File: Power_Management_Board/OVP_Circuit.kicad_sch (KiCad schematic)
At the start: 4 parts, among them Q2 DMG3406L-7, U4 TPS2400

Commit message: Finished USB-C Power Board Design
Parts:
- C10: footprint (none) -> Capacitor_SMD:C_0603_1608Metric_Pad1.08x0.95mm_HandSolder
- D5: value D_Zener -> NC
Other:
- note added: "30V Tolerant"
- note added: "Components need to be at least 20V tolerant"
- note added: "Zener Diode attenuates the voltage spike from an inductive power supply when load is disconnected. Most likely optional"
- note removed: "Zener Diode attenuates the voltage spike from an inductive power supply when load is disconnected."
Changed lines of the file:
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@@
+		)
+	)
+	(text "30V Tolerant"
+		(exclude_from_sim no)
+		(at 114.808 46.736 0)
+		(effects
+			(font
+				(size 1.27 1.27)
+			)
 		)
 	)
@@
 		)
 	)
-	(text "Zener Diode attenuates the voltage\nspike from an inductive power \nsupply when load is disconnected."
+	(text "Components need to be \nat least 20V tolerant"
 		(exclude_from_sim no)
-		(at 27.94 67.31 0)
+		(at 67.31 44.704 0)
+		(effects
+			(font
+				(size 1.27 1.27)
+			)
+		)
+	)
+	(text "Zener Diode attenuates the voltage\nspike from an inductive power \nsupply when load is disconnected.\nMost likely optional"
+		(exclude_from_sim no)
+		(at 26.924 70.612 0)
 		(effects
 			(font
@@
 			)
 		)
-		(property "Footprint" ""
+		(property "Footprint" "Capacitor_SMD:C_0603_1608Metric_Pad1.08x0.95mm_HandSolder"
 			(at 68.58 54.61 0)
 			(effects
@@
 			)
 		)
-		(property "Value" "D_Zener"
+		(property "Value" "NC"
 			(at 49.53 57.15 90)
 			(effects

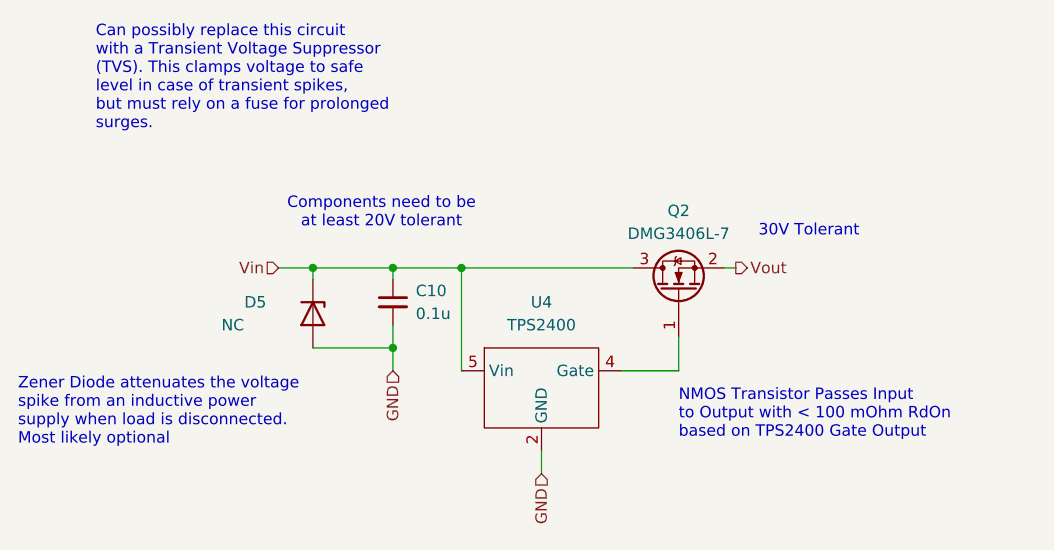
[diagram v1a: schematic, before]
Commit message: Raspberry Pi Board Added
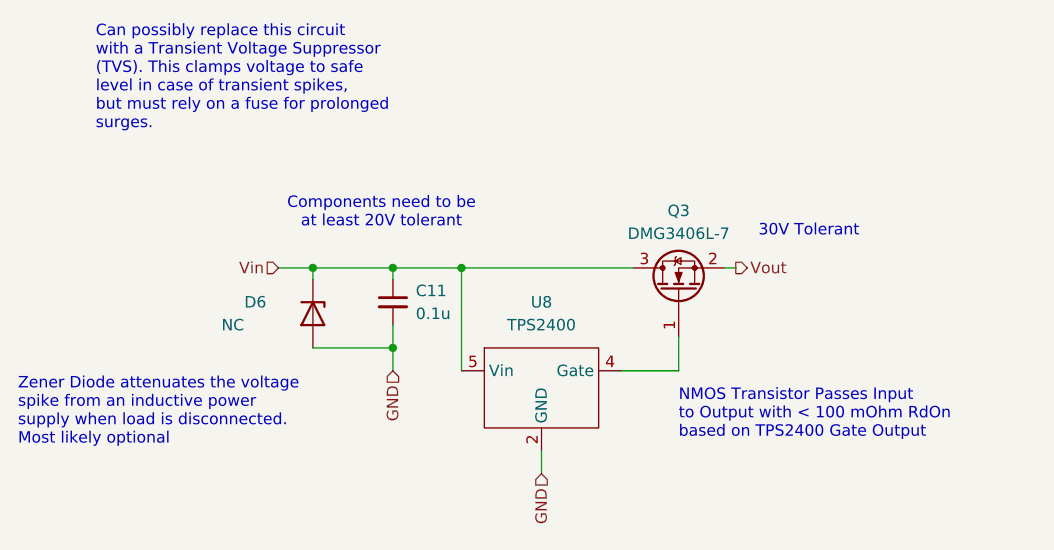
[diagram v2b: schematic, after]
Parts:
- D6: renamed from D5; footprint (none) -> Diode_SMD:D_SOD-123
- renumbered C10 to C11, Q2 to Q3, U4 to U8
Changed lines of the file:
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@@
 		(dnp no)
 		(fields_autoplaced yes)
-		(property "Reference" "C10"
+		(property "Reference" "C11"
 			(at 71.12 53.3463 0)
 			(effects
@@
 		)
 		(instances
-			(project "Power_Management_Board"
-				(path "/ccfc25ad-76bc-4178-a006-8e1d6746309e/3a16a73b-a27b-416f-bc73-9c1f5fba4942"
-					(reference "C10")
+			(project "Raspi_Zero_TFT_Interface"
+				(path "/9fcf58ec-9ad6-40d8-a93b-d0fc15c15838/50d4a57d-354f-4afa-869e-4e71aa380902/217d63bb-6b6c-40b3-9e5b-229da7cf0df5"
+					(reference "C11")
 					(unit 1)
 				)
@@
 		(on_board yes)
 		(dnp no)
-		(property "Reference" "D5"
+		(property "Reference" "D6"
 			(at 52.07 54.61 90)
 			(effects
@@
 			)
 		)
-		(property "Footprint" ""
+		(property "Footprint" "Diode_SMD:D_SOD-123"
 			(at 59.69 55.88 0)
 			(effects
@@
 		)
 		(instances
-			(project "Power_Management_Board"
-				(path "/ccfc25ad-76bc-4178-a006-8e1d6746309e/3a16a73b-a27b-416f-bc73-9c1f5fba4942"
-					(reference "D5")
+			(project "Raspi_Zero_TFT_Interface"
+				(path "/9fcf58ec-9ad6-40d8-a93b-d0fc15c15838/50d4a57d-354f-4afa-869e-4e71aa380902/217d63bb-6b6c-40b3-9e5b-229da7cf0df5"
+					(reference "D6")
 					(unit 1)
 				)
@@
 		(dnp no)
 		(fields_autoplaced yes)
-		(property "Reference" "U4"
+		(property "Reference" "U8"
 			(at 85.09 54.61 0)
 			(effects
@@
 		)
 		(instances
-			(project "Power_Management_Board"
-				(path "/ccfc25ad-76bc-4178-a006-8e1d6746309e/3a16a73b-a27b-416f-bc73-9c1f5fba4942"
-					(reference "U4")
+			(project "Raspi_Zero_TFT_Interface"
+				(path "/9fcf58ec-9ad6-40d8-a93b-d0fc15c15838/50d4a57d-354f-4afa-869e-4e71aa380902/217d63bb-6b6c-40b3-9e5b-229da7cf0df5"
+					(reference "U8")
 					(unit 1)
 				)
@@
 		(dnp no)
 		(fields_autoplaced yes)
-		(property "Reference" "Q2"
+		(property "Reference" "Q3"
 			(at 100.33 44.45 90)
 			(effects
@@
 		)
 		(instances
-			(project "Power_Management_Board"
-				(path "/ccfc25ad-76bc-4178-a006-8e1d6746309e/3a16a73b-a27b-416f-bc73-9c1f5fba4942"
-					(reference "Q2")
-					(unit 1)
-				)
+			(project "Raspi_Zero_TFT_Interface"
+				(path "/9fcf58ec-9ad6-40d8-a93b-d0fc15c15838/50d4a57d-354f-4afa-869e-4e71aa380902/217d63bb-6b6c-40b3-9e5b-229da7cf0df5"
+					(reference "Q3")
+					(unit 1)
+				)
